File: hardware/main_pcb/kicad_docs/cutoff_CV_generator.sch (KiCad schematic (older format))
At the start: 13 parts, among them U5 TL072

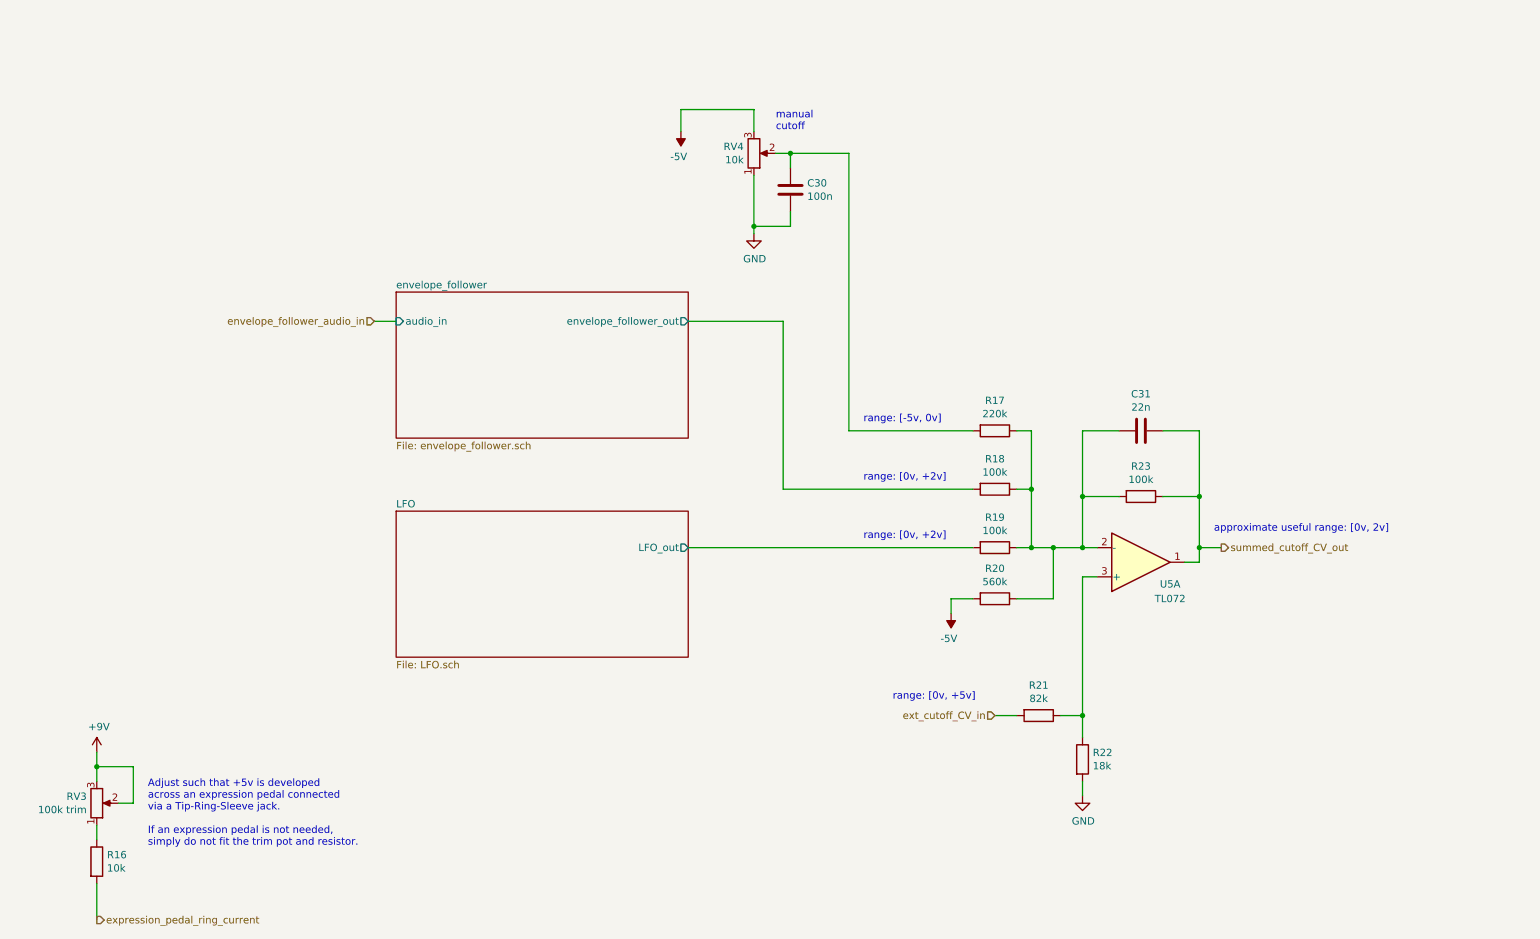
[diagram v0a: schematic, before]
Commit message: add LED driver, change LED to 5mm
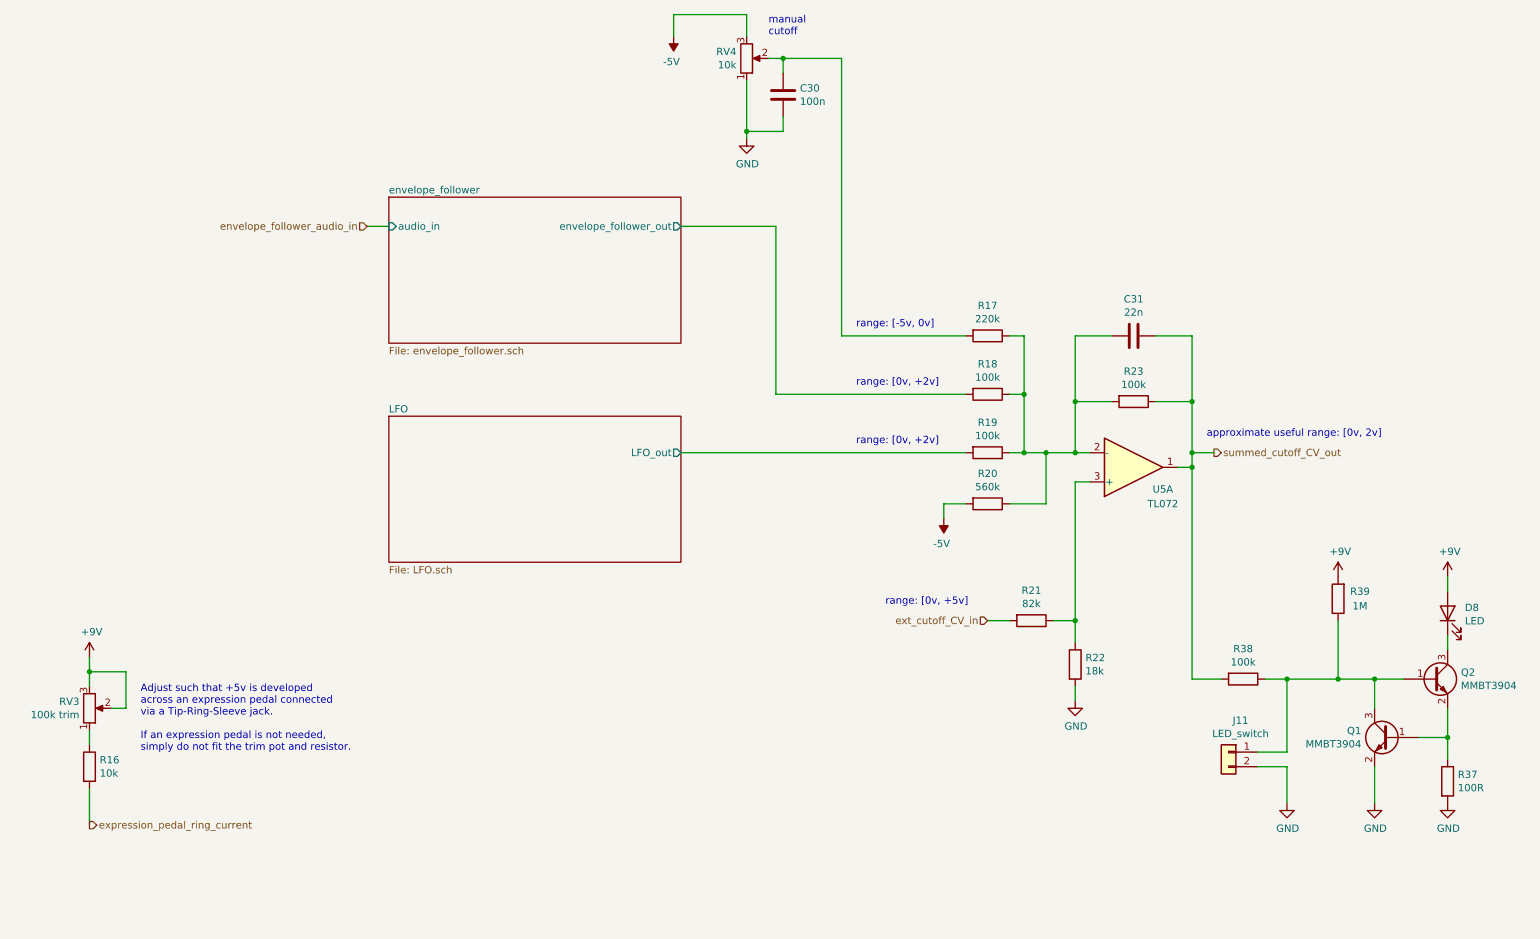
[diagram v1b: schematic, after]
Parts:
- added D8: LED, LED_THT:LED_D5.0mm, symbol Device:LED
- added J11: LED_switch, Connector_PinHeader_2.54mm:PinHeader_1x02_P2.54mm_Vertical, symbol Connector_Generic:Conn_01x02
- added Q1, Q2: MMBT3904, Package_TO_SOT_SMD:SOT-23, symbol Transistor_BJT:MMBT3904
- added R37: 100R, Resistor_SMD:R_0805_2012Metric, symbol Device:R
- added R38: 100k, Resistor_SMD:R_0805_2012Metric, symbol Device:R
- added R39: 1M, Resistor_SMD:R_0805_2012Metric, symbol Device:R
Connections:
- net +9V: now also D8.2 (A), R39.2
- net GND: now also J11.2 (Pin_2), Q1.2 (E), R37.2
- net summed_cutoff_CV_out: now also R38.2
- new net: Q1.1 (B), Q2.2 (E), R37.1
- new net: J11.1 (Pin_1), Q1.3 (C), Q2.1 (B), R38.1, R39.1
- new net: D8.1 (K), Q2.3 (C)
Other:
- moved on the sheet: C30, C31, R16, R17, R18, R19, R20, R21, R22, R23, RV3, RV4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

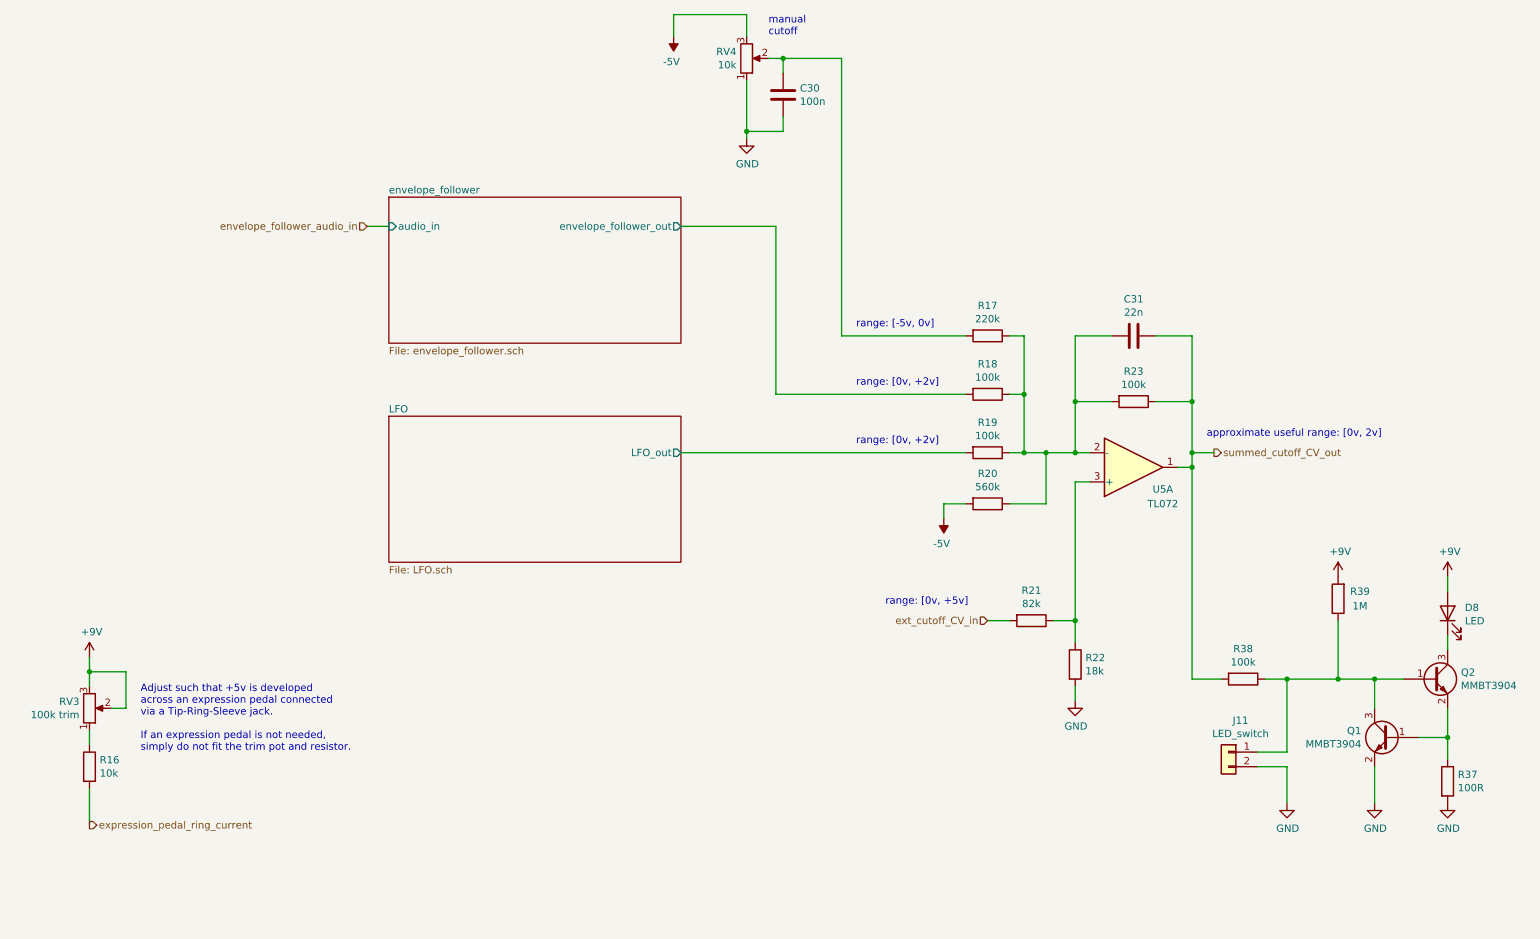
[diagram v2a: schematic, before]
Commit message: center envelope follower around +1v, tidy up
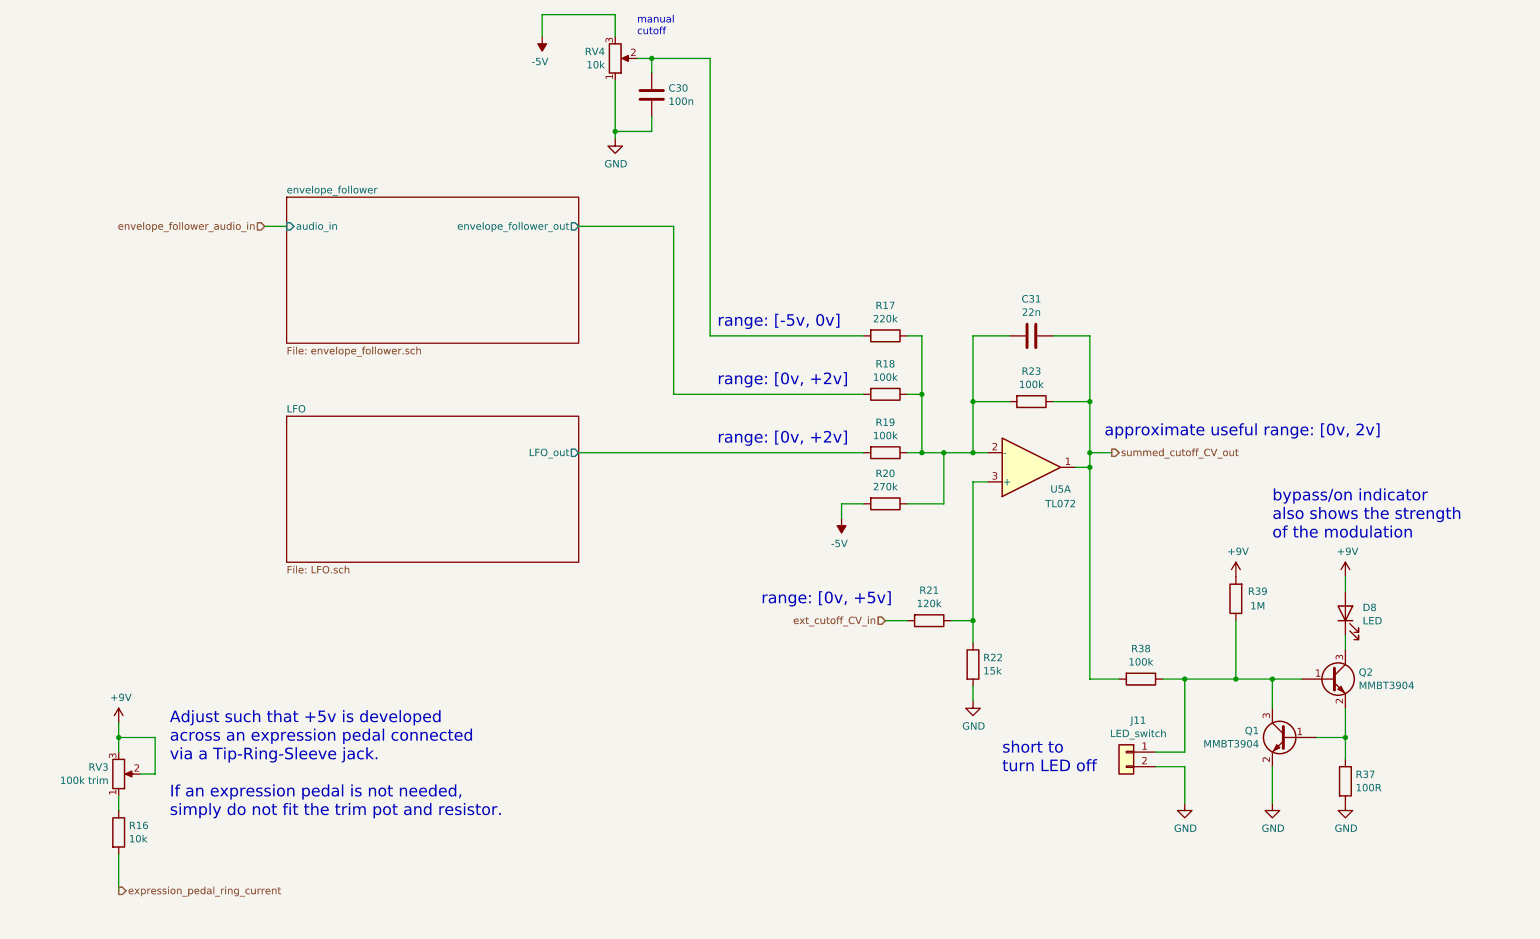
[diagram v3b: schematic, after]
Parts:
- R20: value 560k -> 270k
- R21: value 82k -> 120k
- R22: value 18k -> 15k
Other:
- note added: "bypass/on indicator\nalso shows the strength \nof the modulation"
- note added: "short to \nturn LED off"
- moved on the sheet: C30, C31, D8, J11, Q1, Q2, R16, R17, R18, R19, R20, R21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
